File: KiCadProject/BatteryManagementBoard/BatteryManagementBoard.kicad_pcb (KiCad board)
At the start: 2 copper layers, 45 x 45 mm, 0 parts

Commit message: jan 4
Signed-off-by: Eldalote.Electronics <Eldalote.Electronics@gmail.com>
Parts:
- added C301: 10u, Capacitor_SMD:C_0805_2012Metric, F.Cu at (148.8, 103.2)
- added C302: 10u, Capacitor_SMD:C_0805_2012Metric, F.Cu at (151.4, 109.3)
- added C303: 10u, Capacitor_SMD:C_0805_2012Metric, F.Cu at (153.2, 103.2)
- added C304: 10u, Capacitor_SMD:C_0805_2012Metric, F.Cu at (142.5, 109.5)
- added C305: 10u, Capacitor_SMD:C_0805_2012Metric, F.Cu at (142.5, 112.5)
- added C306: 10u, Capacitor_SMD:C_0805_2012Metric, F.Cu at (157.7, 100.2)
- added C307: 10u, Capacitor_SMD:C_0805_2012Metric, F.Cu at (146.9, 112.5)
- added C308: 33n, Capacitor_SMD:C_0402_1005Metric, F.Cu at (166.3, 103.7)
- added C309: 33n, Capacitor_SMD:C_0402_1005Metric, F.Cu at (156.3, 113.7)
- added C310: 10n, Capacitor_SMD:C_0402_1005Metric, F.Cu at (168.2, 99.7)
- added C311: 1n, Capacitor_SMD:C_0402_1005Metric, F.Cu at (157.4, 111.3)
- added C312: 47n, Capacitor_SMD:C_0402_1005Metric, F.Cu at (168.2, 101.7)
- added C313: 47n, Capacitor_SMD:C_0402_1005Metric, F.Cu at (159.0, 108.8)
- added C314: 10u, Capacitor_SMD:C_0805_2012Metric, F.Cu at (153.2, 100.2)
- added C315: 10u, Capacitor_SMD:C_0805_2012Metric, F.Cu at (155.8, 106.3)
- added C316: 10u, Capacitor_SMD:C_0603_1608Metric, F.Cu at (161.9, 102.5)
- added C317: 10u, Capacitor_SMD:C_0805_2012Metric, F.Cu at (157.7, 103.2)
- added C318: 10u, Capacitor_SMD:C_0805_2012Metric, F.Cu at (146.9, 109.5)
- added C319: 10u, Capacitor_SMD:C_0805_2012Metric, F.Cu at (148.8, 100.2)
- added C320: 10u, Capacitor_SMD:C_0805_2012Metric, F.Cu at (151.4, 106.3)
- added C321: 10u, Capacitor_SMD:C_0805_2012Metric, F.Cu at (146.9, 106.5)
- added C322: 1u, Capacitor_SMD:C_0603_1608Metric, F.Cu at (155.6, 109.0)
- added C323: 100n, Capacitor_SMD:C_0402_1005Metric, F.Cu at (153.4, 114.3)
- added C324: 10u, Capacitor_SMD:C_0805_2012Metric, F.Cu at (142.5, 106.5)
- added C325: 1u, Capacitor_SMD:C_0603_1608Metric, F.Cu at (160.0, 106.0)
- added C326: 1u, Capacitor_SMD:C_0603_1608Metric, F.Cu at (161.9, 100.0)
- added C327: 33p, Capacitor_SMD:C_0402_1005Metric, F.Cu at (150.6, 114.3)
- added C328: 1800p, Capacitor_SMD:C_0402_1005Metric, F.Cu at (163.5, 104.7)
- added C329: 15p, Capacitor_SMD:C_0402_1005Metric, F.Cu at (161.9, 108.2)
- added C330: 680p, Capacitor_SMD:C_0402_1005Metric, F.Cu at (165.3, 99.7)
- added C331: 2u2, Capacitor_SMD:C_0603_1608Metric, F.Cu at (151.1, 112.0)
- added C332: 100p, Capacitor_SMD:C_0402_1005Metric, F.Cu at (165.3, 101.7)
- added C333: 100p, Capacitor_SMD:C_0402_1005Metric, F.Cu at (154.6, 111.8)
- added C401: 22u, Capacitor_SMD:CP_Elec_5x5.3, F.Cu at (197.0, 78.2)
- added C402: 100n, Capacitor_SMD:C_0402_1005Metric, F.Cu at (194.0, 82.7)
- added C403: 10u, Capacitor_SMD:C_0805_2012Metric, F.Cu at (182.6, 84.4)
- added J201: USB-C-2.0, Imported:GCT_USB4120-03-C_REVA, F.Cu at (150.2, 84.5)
- added J202: XT30, Eldalote-footprints:XT30, F.Cu at (139.8, 86.8)
- added J203: Conn_02x05, Connector_PinHeader_1.27mm:PinHeader_2x05_P1.27mm_Vertical_SMD, F.Cu at (132.8, 99.8)
- added J204: XT60, Eldalote-footprints:XT60, F.Cu at (149.8, 116.5)
- added J205: Conn_02x05, Connector_PinHeader_1.27mm:PinHeader_2x05_P1.27mm_Vertical_SMD, F.Cu at (179.5, 98.8)
- added J206: Conn_01x02_Male, Connector_PinHeader_1.27mm:PinHeader_1x02_P1.27mm_Vertical, F.Cu at (155.2, 85.2)
- added U301: BQ25713, Package_DFN_QFN:Texas_S-PWQFN-N32_EP2.8x2.8mm, F.Cu at (143.0, 99.2)
- added U401: BD433M5FP, Package_TO_SOT_SMD:TO-252-3_TabPin4, F.Cu at (163.2, 91.8)

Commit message: Tweaking
Signed-off-by: Eldalote.Electronics <Eldalote.Electronics@gmail.com>
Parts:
- added C501: 10u, Capacitor_SMD:C_0805_2012Metric, F.Cu at (74.0, 115.2)
- added C502: 1u, Capacitor_SMD:C_0603_1608Metric, F.Cu at (73.8, 118.0)
- added C503: 220p, Capacitor_SMD:C_0402_1005Metric, F.Cu at (77.2, 117.7)
- added C504: 220p, Capacitor_SMD:C_0402_1005Metric, F.Cu at (80.1, 116.7)
- added J207: Conn_01x05_Male, Connector_PinHeader_1.27mm:PinHeader_1x05_P1.27mm_Vertical_SMD_Pin1Left, F.Cu at (150.2, 88.8)
- added J208: JST_B5B_XH, Connector_JST:JST_XH_B5B-XH-A_1x05_P2.50mm_Vertical, B.Cu at (145.2, 83.5)
- added R201: 5k1, Resistor_SMD:R_0402_1005Metric, F.Cu at (76.1, 108.8)
- added R202: 5k1, Resistor_SMD:R_0402_1005Metric, F.Cu at (73.2, 108.8)
- added R301: 10m, Resistor_SMD:R_1206_3216Metric, F.Cu at (96.8, 104.9)
- added R302: 4R99, Resistor_SMD:R_0402_1005Metric, F.Cu at (104.1, 106.9)
- added R303: 4R99, Resistor_SMD:R_0402_1005Metric, F.Cu at (101.0, 104.9)
- added R304: 10m, Resistor_SMD:R_1206_3216Metric, F.Cu at (96.8, 101.6)
- added R305: 10R, Resistor_SMD:R_0402_1005Metric, F.Cu at (109.7, 103.0)
- added R306: 10R, Resistor_SMD:R_0402_1005Metric, F.Cu at (106.8, 103.0)
- added R307: 10R, Resistor_SMD:R_0402_1005Metric, F.Cu at (98.3, 107.5)
- added R308: 10R, Resistor_SMD:R_0402_1005Metric, F.Cu at (101.0, 101.0)
- added R309: 100k, Resistor_SMD:R_0402_1005Metric, F.Cu at (106.8, 101.0)
- added R310: 174k, Resistor_SMD:R_0402_1005Metric, F.Cu at (103.9, 104.9)
- added R311: 300k, Resistor_SMD:R_0402_1005Metric, F.Cu at (103.9, 103.0)
- added R312: 100k, Resistor_SMD:R_0402_1005Metric, F.Cu at (103.9, 101.0)
- added R313: 100k, Resistor_SMD:R_0402_1005Metric, F.Cu at (101.0, 103.0)
- added R314: 40K2, Resistor_SMD:R_0402_1005Metric, F.Cu at (109.7, 101.0)
- added R315: 10k, Resistor_SMD:R_0402_1005Metric, F.Cu at (101.2, 106.9)
- added R316: 10k, Resistor_SMD:R_0402_1005Metric, F.Cu at (106.8, 104.9)
- added R317: 10k, Resistor_SMD:R_0402_1005Metric, F.Cu at (101.2, 108.9)
- added R318: 137k, Resistor_SMD:R_0402_1005Metric, F.Cu at (95.4, 107.5)
- added R401: 649R, Resistor_SMD:R_0402_1005Metric, F.Cu at (95.4, 114.2)
- added R501: 200k, Resistor_SMD:R_0402_1005Metric, F.Cu at (77.7, 114.7)
- J206: footprint Connector_PinHeader_1.27mm:PinHeader_1x02_P1.27mm_Vertical -> Connector_PinHeader_1.27mm:PinHeader_1x02_P1.27mm_Vertical_SMD_Pin1Left
- moved C301 39.0 mm to (142.2, 141.7)
- moved C303 39.0 mm to (146.6, 141.7)
- moved C308 39.0 mm to (159.8, 142.2)
- moved C310 39.0 mm to (161.6, 138.2)
- moved C312 39.0 mm to (161.6, 140.2)
- moved C313 39.0 mm to (152.5, 147.2)
- moved C316 39.0 mm to (155.3, 141.0)
- moved C317 39.0 mm to (151.1, 141.7)
- moved C321 39.0 mm to (140.3, 145.0)
- moved C324 39.0 mm to (135.9, 145.0)
- moved C329 39.0 mm to (155.3, 146.7)
- moved C330 39.0 mm to (158.8, 138.2)
- moved C332 39.0 mm to (158.8, 140.2)
- moved U301 39.0 mm to (136.4, 137.7)
- moved C331 39.0 mm to (144.6, 150.5)
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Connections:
- J201 pad S2: unconnected-(J201-PadS1) -> unconnected-(J201-PadS2)
- J201 pad S3: unconnected-(J201-PadS1) -> unconnected-(J201-PadS3)
- J201 pad S4: unconnected-(J201-PadS1) -> unconnected-(J201-PadS4)

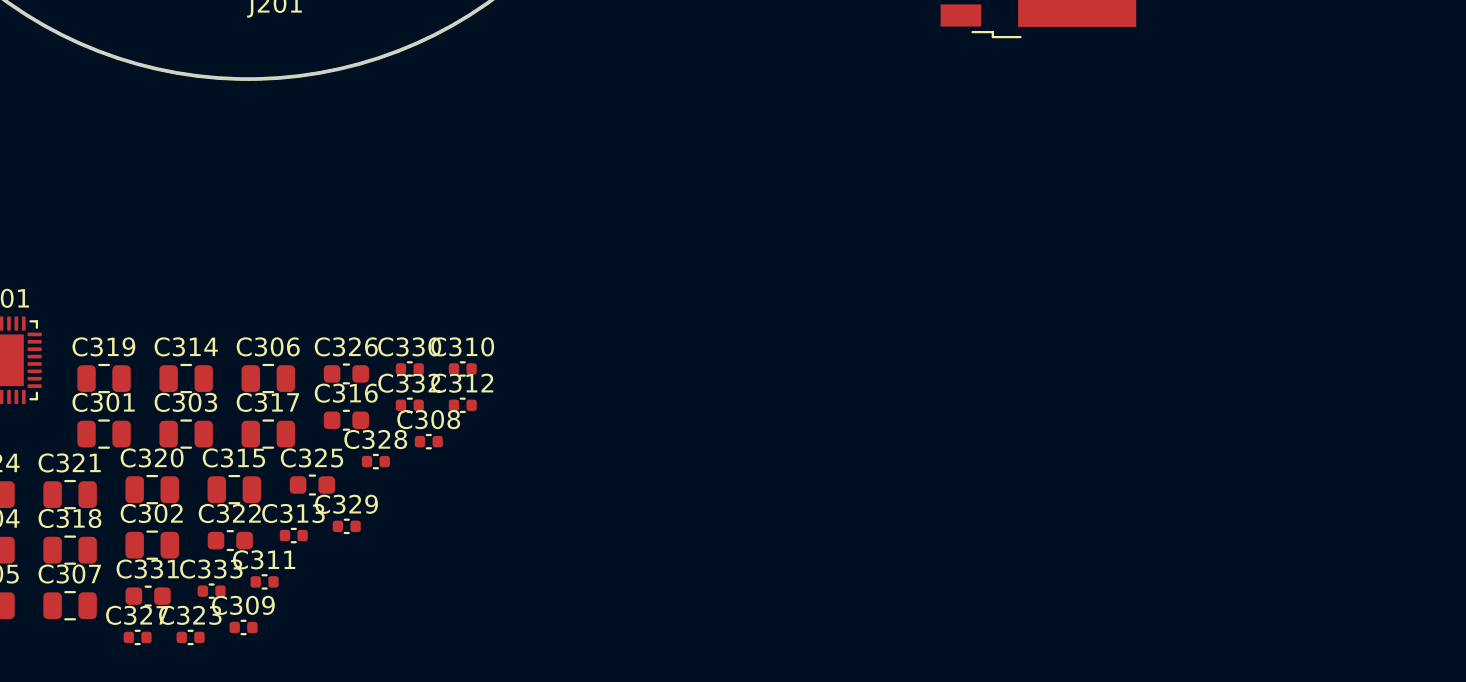
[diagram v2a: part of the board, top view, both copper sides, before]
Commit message: Final touches before component order and PCB layout
Signed-off-by: Eldalote.Electronics <Eldalote.Electronics@gmail.com>
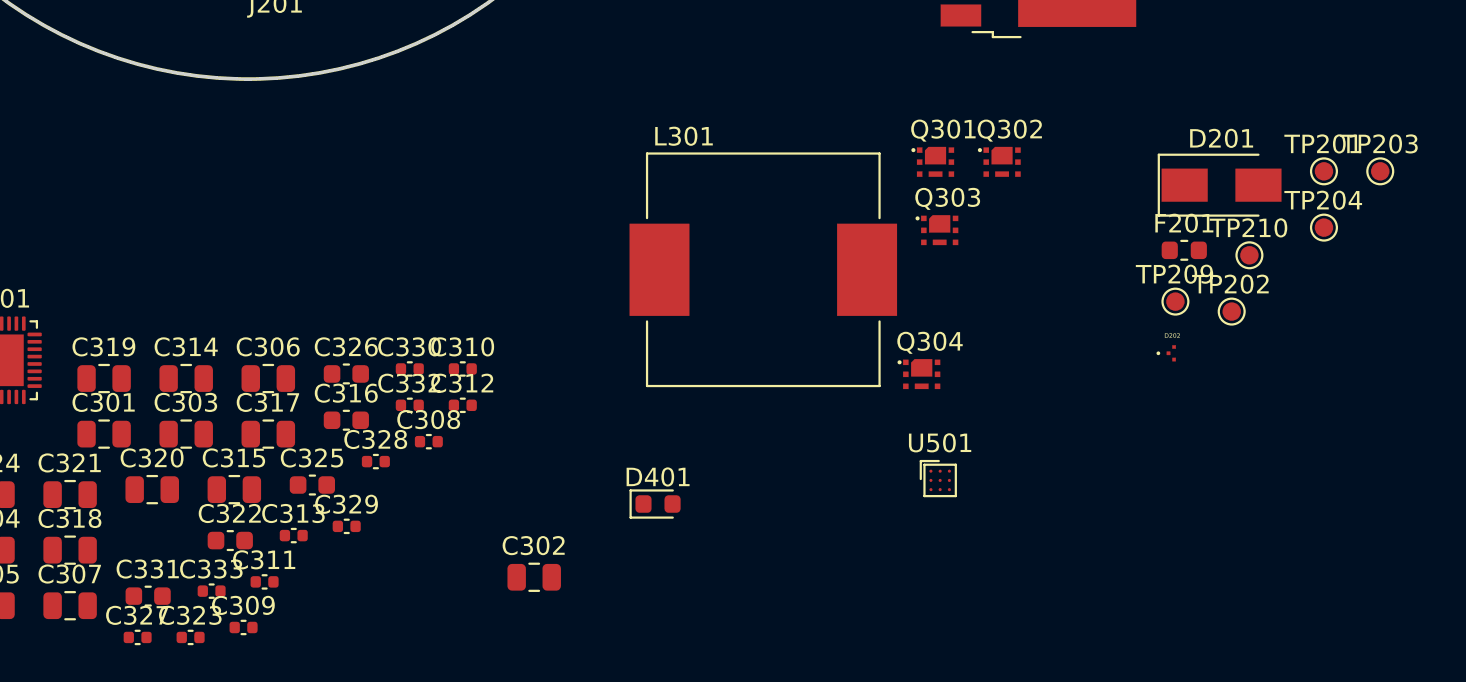
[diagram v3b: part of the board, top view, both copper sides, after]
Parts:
- added D201: 20v tvs, Diode_SMD:D_SMA, F.Cu at (202.8, 128.2)
- added D202: TVS_Dual_USB, Imported:IC_ESD122DMXR, F.Cu at (200.0, 137.4)
- added D401: GREEN LED, LED_SMD:LED_0603_1608Metric, F.Cu at (172.2, 145.5)
- added F201: Fuse 32V 5A, Fuse:Fuse_0603_1608Metric, F.Cu at (200.7, 131.8)
- added L301: 2u2, Eldalote-footprints:SRP-1265C, F.Cu at (177.9, 132.8)
- added Q301: NFET_Gatenames, Eldalote-footprints:SSM6K504, F.Cu at (187.2, 127.0)
- added Q302: NFET_Gatenames, Eldalote-footprints:SSM6K504, F.Cu at (190.9, 127.0)
- added Q303: NFET_Gatenames, Eldalote-footprints:SSM6K504, F.Cu at (187.5, 130.7)
- added Q304: NFET_Gatenames, Eldalote-footprints:SSM6K504, F.Cu at (186.5, 138.5)
- added TP201: TestPoint, TestPoint:TestPoint_Pad_D1.0mm, F.Cu at (208.3, 127.5)
- added TP202: TestPoint, TestPoint:TestPoint_Pad_D1.0mm, F.Cu at (203.3, 135.1)
- added TP203: TestPoint, TestPoint:TestPoint_Pad_D1.0mm, F.Cu at (211.3, 127.5)
- added TP204: TestPoint, TestPoint:TestPoint_Pad_D1.0mm, F.Cu at (208.3, 130.6)
- added TP209: TestPoint, TestPoint:TestPoint_Pad_D1.0mm, F.Cu at (200.2, 134.6)
- added TP210: TestPoint, TestPoint:TestPoint_Pad_D1.0mm, F.Cu at (204.3, 132.1)
- added U501: TUSB422, Package_BGA:Texas_DSBGA-9_1.4715x1.4715mm_Layout3x3_P0.5mm, F.Cu at (187.5, 144.2)
- moved C302 20.8 mm to (165.5, 149.5)

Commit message: Layout on the battery management board
Signed-off-by: Eldalote.Electronics <Eldalote.Electronics@gmail.com>
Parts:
- removed TP202, TP203, TP204, TP209, TP210: TestPoint, TestPoint:TestPoint_Pad_D1.0mm
- added Q305: PMOS_Gatenames, Eldalote-footprints:DFN3x3A_8L_EP1_P, B.Cu at (139.5, 107.9)
- C301, C302, C303, C304, C305, C306, C307, C308, C309, C310, C311, C312, C313, C314, C315, C317, C318, C319, C320, C321, C322, C323, C325, C326, C327, C328, C329, C330, C333, C401, C503, C504, D201, D202, F201, J202, J204, L301, R201, R202, R301, R302, R303, R304, R305, R306, R310, R312, R313, R314, R315, R316, R317, TP201, U301: moved to B.Cu
- C316: footprint Capacitor_SMD:C_0603_1608Metric -> Capacitor_SMD:C_0805_2012Metric; moved to B.Cu
- D401: footprint LED_SMD:LED_0603_1608Metric -> LED_SMD:LED_0805_2012Metric
- Q301, Q302, Q303, Q304: footprint Eldalote-footprints:SSM6K504 -> Eldalote-footprints:DFN3x3A_8L_EP1_P; moved to B.Cu
- R307: value 10R -> 1R; footprint Resistor_SMD:R_0402_1005Metric -> Resistor_SMD:R_0603_1608Metric; moved to B.Cu
- moved C502 97.1 mm to (170.2, 107.2), turned to 90 degrees
- moved C501 94.1 mm to (167.8, 107.0)
- moved C503 92.2 mm to (169.2, 112.2)
- moved R501 90.4 mm to (167.5, 104.5), turned to 180 degrees
- moved R202 89.8 mm to (163.0, 108.2), turned to 90 degrees
- moved C504 87.0 mm to (167.0, 112.2)
- moved R201 86.9 mm to (163.0, 111.5), turned to -90 degrees
- moved C401 70.1 mm to (136.0, 112.8), turned to -90 degrees
- moved R316 66.6 mm to (173.2, 100.8), turned to 90 degrees
- moved R301 63.8 mm to (160.0, 96.5), turned to 90 degrees
- moved Q304 62.6 mm to (140.5, 96.0), turned to -90 degrees
- moved Q303 60.7 mm to (140.5, 92.2), turned to 90 degrees
- moved C402 59.5 mm to (140.2, 108.2), turned to -90 degrees
- moved R307 58.9 mm to (157.2, 106.8), turned to 180 degrees
- moved R303 57.9 mm to (158.2, 96.0), turned to 90 degrees
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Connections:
- net Net-(D401-Pad2) renamed /P4 - 3V3 Regulator/POWER_LED
- net Net-(R310-Pad1) renamed /P3-Charger/ILIM_HIZ
- J203 pad 1: +3V3 -> +3.3V
- J203 pad 2: +3V3 -> +3.3V
- J205 pad 1: +3V3 -> +3.3V
- J205 pad 2: +3V3 -> +3.3V
- U501 pad C3: (no net) -> SDA
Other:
- copper layers 2 -> 6

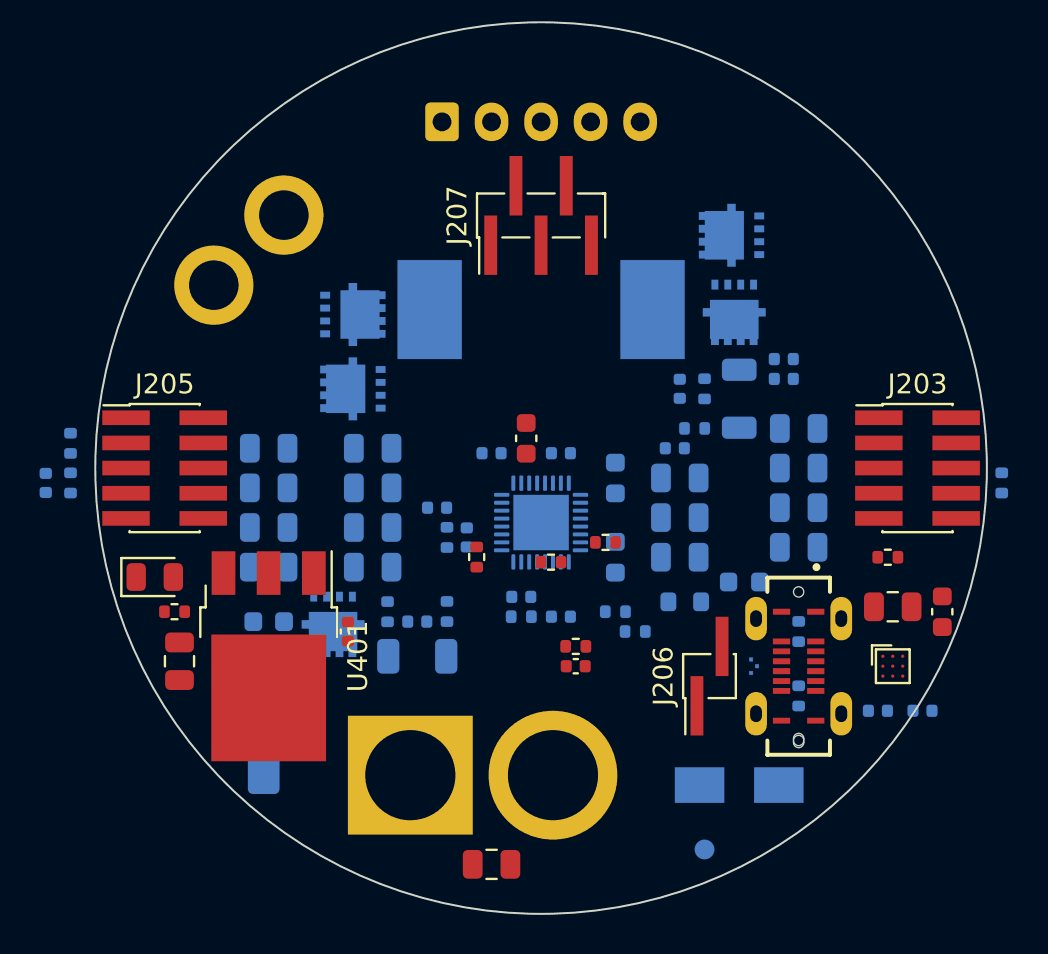
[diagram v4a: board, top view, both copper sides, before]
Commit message: Routed Bat management (replaced TUSB because it physically can't be routed with constraints)
Signed-off-by: Eldalote.Electronics <Eldalote.Electronics@gmail.com>
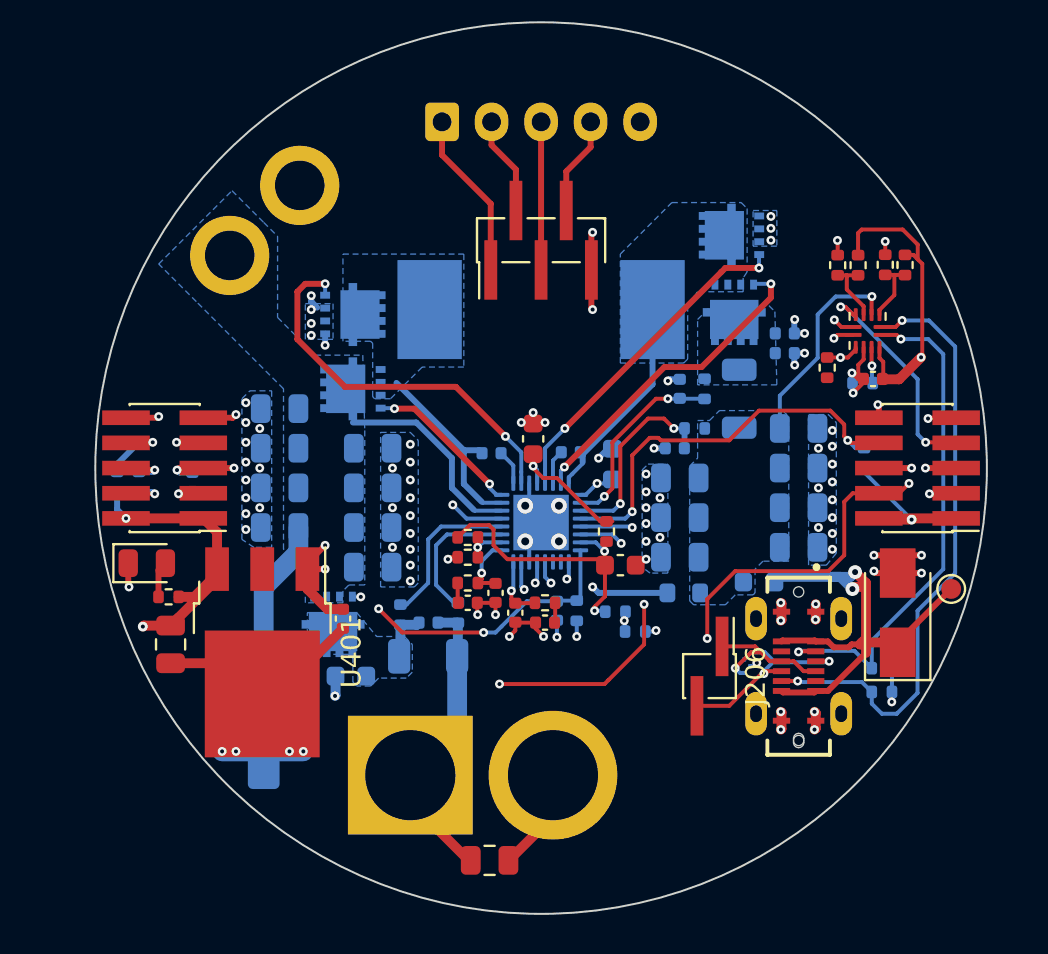
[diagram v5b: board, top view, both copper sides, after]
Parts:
- removed C502: 1u, Capacitor_SMD:C_0603_1608Metric
- removed C503, C504: 220p, Capacitor_SMD:C_0402_1005Metric
- added R502: DNP, Resistor_SMD:R_0402_1005Metric, F.Cu at (165.0, 89.8)
- added R503: 10k, Resistor_SMD:R_0402_1005Metric, F.Cu at (168.4, 89.8)
- added R504: DNP, Resistor_SMD:R_0402_1005Metric, F.Cu at (167.4, 89.7)
- added R505: 10k, Resistor_SMD:R_0402_1005Metric, B.Cu at (166.2, 95.7)
- added R506: 10k, Resistor_SMD:R_0402_1005Metric, F.Cu at (164.4, 94.9)
- C326, C327, C328, C329, C330, D201, R314, R315, TP201: moved to F.Cu
- C332, R318: moved to B.Cu
- C501: value 10u -> 100n; footprint Capacitor_SMD:C_0805_2012Metric -> Capacitor_SMD:C_0402_1005Metric
- R501: value 200k -> 10k
- U501: value TUSB422 -> PTN5150; footprint Package_BGA:Texas_DSBGA-9_1.4715x1.4715mm_Layout3x3_P0.5mm -> Package_DFN_QFN:Texas_X2QFN-12_1.6x1.6mm_P0.4mm
- moved TP201 18.1 mm to (170.7, 106.1), turned to 0 degrees
- moved U501 17.0 mm to (166.5, 93.1), turned to 180 degrees
- moved R501 14.8 mm to (166.0, 89.8), turned to 90 degrees
- moved D201 11.8 mm to (168.0, 107.3), turned to 90 degrees
- moved C501 11.5 mm to (166.8, 95.5), turned to 180 degrees
- moved C314 8.02 mm to (136.8, 97.0)
- moved C333 7.40 mm to (132.4, 100.7)
- moved R316 7.06 mm to (166.3, 99.5), turned to -90 degrees
- moved C330 5.04 mm to (146.3, 106.8), turned to 0 degrees
- moved C322 4.98 mm to (140.4, 110.5)
- moved R202 4.59 mm to (167.2, 110.1), turned to 0 degrees
- moved R309 4.38 mm to (146.3, 103.5), turned to 180 degrees
- moved R201 4.20 mm to (167.2, 111.3), turned to 0 degrees
- moved R313 3.96 mm to (129.7, 100.7), turned to -90 degrees
- moved C329 3.15 mm to (147.7, 106.3), turned to -90 degrees
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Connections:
- C501 pad 1: VBUS -> +3.3V
- J203 pad 7: TUS_INT_N -> USBC_INT
- J203 pad 9: GND -> PTN_ID
- R501 pad 1: +3.3V -> /P5-TUSB422 (Optional)/PTN_ADR
- R501 pad 2: TUS_INT_N -> +3.3V
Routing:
- net +3.3V: track 0.00 -> 110.0 mm, vias 0 -> 4
- net GND: track 0.00 -> 76.9 mm, vias 0 -> 106
- net BQ_EN_OTG: track 0.00 -> 42.9 mm, vias 0 -> 4
- net SCL: track 0.00 -> 40.9 mm, vias 0 -> 4
- net SDA: track 0.00 -> 38.7 mm, vias 0 -> 3
- net BQ_CMPOUT: track 0.00 -> 35.9 mm, vias 0 -> 2
- net BQ_IADPT: track 0.00 -> 31.7 mm, vias 0 -> 3
- net CC2: track 0.00 -> 31.0 mm, vias 0 -> 2
- net BQ_IBAT: track 0.00 -> 30.3 mm, vias 0 -> 2
- net /P2-Connectors/VBUS_connector: track 0.00 -> 26.9 mm, vias 0 -> 2
- net CC1: track 0.00 -> 25.8 mm, vias 0 -> 2
- net VOUT: track 0.00 -> 23.9 mm, vias 0 -> 2
- net BQ_CHRG_OK: track 0.00 -> 21.1 mm, vias 0 -> 2
- net /P3-Charger/LODRV2: track 0.00 -> 19.8 mm, vias 0 -> 2
- net /P3-Charger/LODRV1: track 0.00 -> 17.0 mm, vias 0 -> 2
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- added copper zone on B.Cu, net /P3-Charger/SW1
- added copper zone on B.Cu, net /P3-Charger/SW2
- added copper zone on B.Cu, net /P3-Charger/VBAT-ps
- added copper zone on B.Cu, net /P3-Charger/VBUS-ps
- added copper zone on B.Cu, net GND
- added copper zone on In1.Cu, net GND
- added copper zone on In3.Cu, net GND
- added copper zone on In4.Cu, net GND
- added copper zone on B.Cu, net VBUS
- added copper zone on B.Cu, net VOUT
